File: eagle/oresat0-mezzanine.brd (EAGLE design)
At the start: 80 x 74 mm, 22 parts, among them J1 R107064070, J10 R107064070, J2 R107064070, J3 R107064070, J4 R107064070, J5 R107064070, J6 R107064070, J7 R107064070, J8 R107064070, J9 R107064070, U1 QBA-07+, U2 QBA-07+, U3 QBA-07+, U7 QCN-27D+, U8 QCN-27D+, U9 QCN-27D+

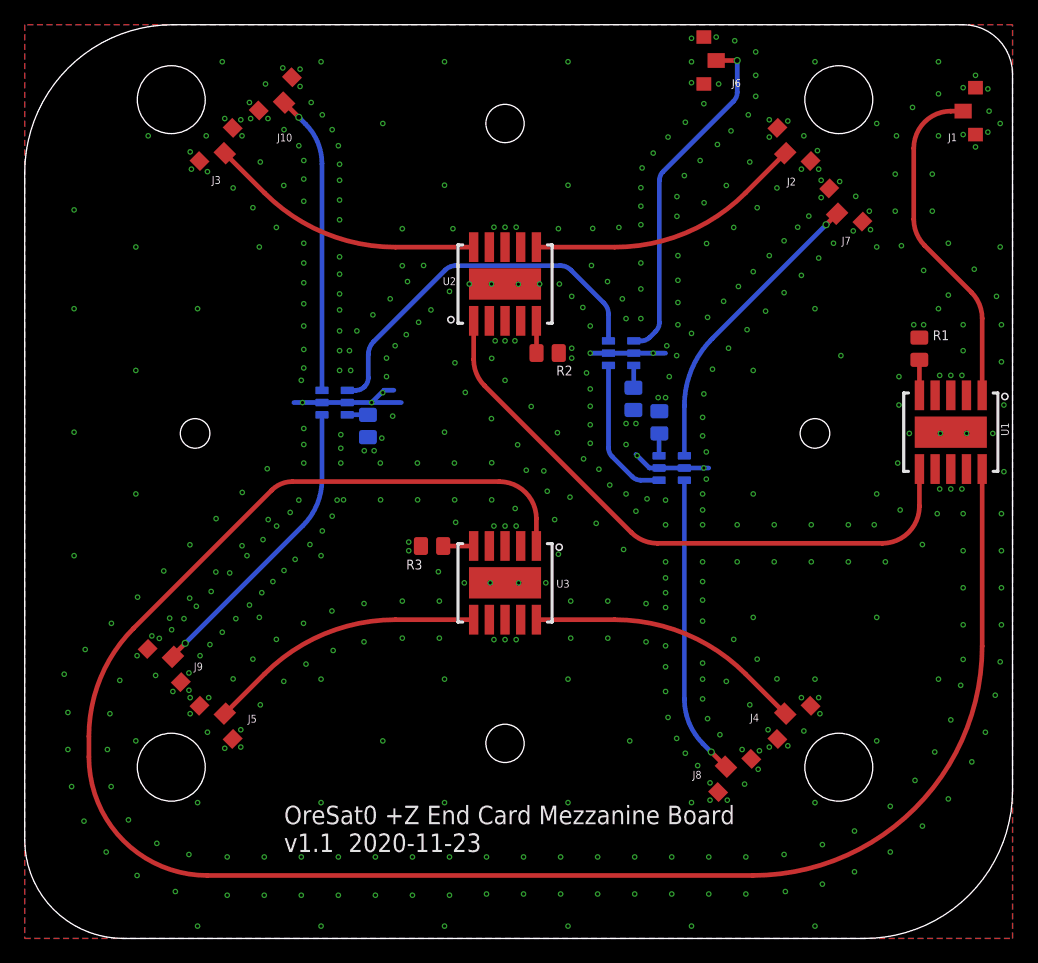
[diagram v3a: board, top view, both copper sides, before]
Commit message: Small tweaks; reduced mezanine board size. Added flight tags. Off to fab!
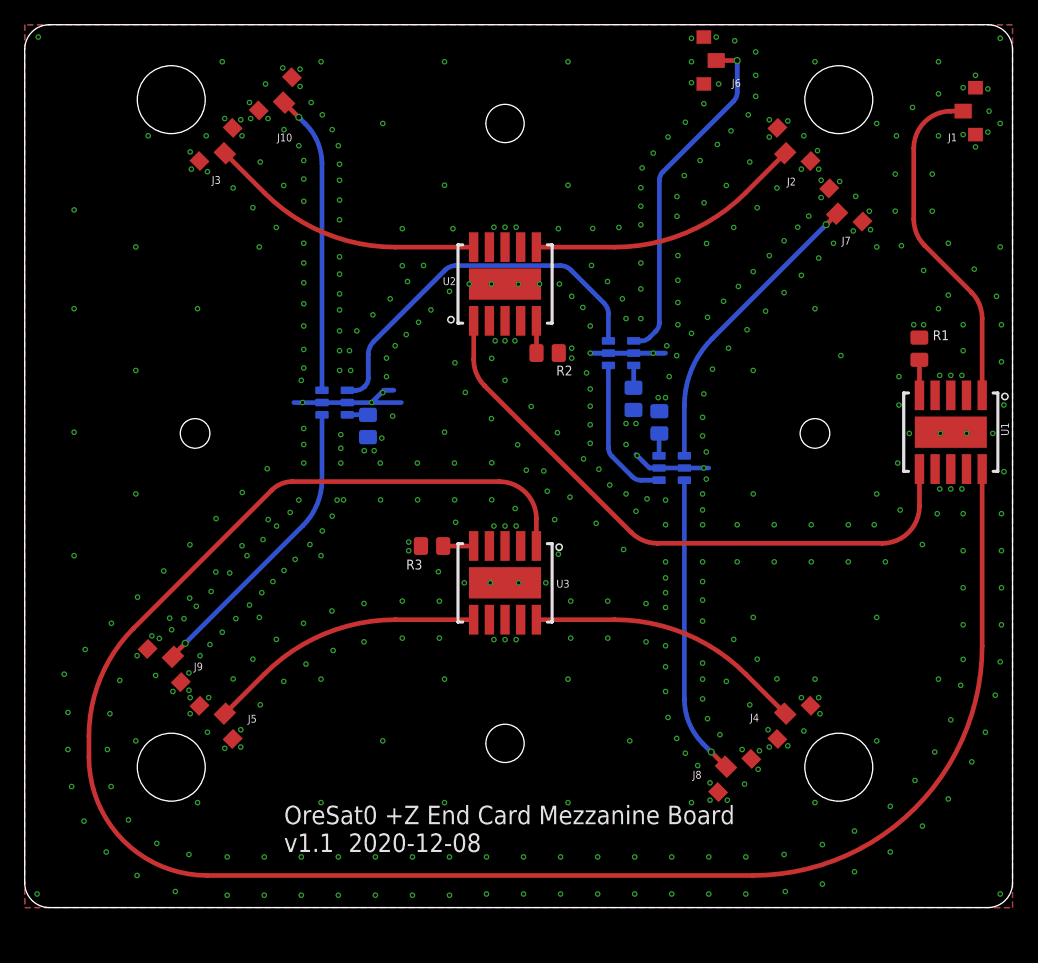
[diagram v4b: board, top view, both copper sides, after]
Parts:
- added U$1: FLIGHMARKERNEW, oresat-flight-marker:FLIGHTMARKER_NEW_BOARDS
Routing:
- net GND: vias 534 -> 532
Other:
- board size 80 x 74 mm -> 80 x 71.5 mm
- board text added: "OreSat0 +Z End Card Mezzanine Board v1.1 2020-12-08"
- board text removed: "OreSat0 +Z End Card Mezzanine Board v1.1 2020-11-23"
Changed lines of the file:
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@@
 <layer number="14" name="Route14" color="22" fill="1" visible="no" active="no"/>
 <layer number="15" name="Route15" color="23" fill="1" visible="no" active="yes"/>
-<layer number="16" name="Bottom" color="1" fill="1" visible="no" active="yes"/>
+<layer number="16" name="Bottom" color="1" fill="1" visible="yes" active="yes"/>
 <layer number="17" name="Pads" color="2" fill="1" visible="yes" active="yes"/>
 <layer number="18" name="Vias" color="2" fill="1" visible="yes" active="yes"/>
@@
 <layer number="20" name="Dimension" color="24" fill="1" visible="yes" active="yes"/>
 <layer number="21" name="tPlace" color="7" fill="1" visible="yes" active="yes"/>
-<layer number="22" name="bPlace" color="7" fill="1" visible="no" active="yes"/>
+<layer number="22" name="bPlace" color="7" fill="1" visible="yes" active="yes"/>
 <layer number="23" name="tOrigins" color="15" fill="1" visible="yes" active="yes"/>
-<layer number="24" name="bOrigins" color="15" fill="1" visible="no" active="yes"/>
+<layer number="24" name="bOrigins" color="15" fill="1" visible="yes" active="yes"/>
 <layer number="25" name="tNames" color="7" fill="1" visible="yes" active="yes"/>
-<layer number="26" name="bNames" color="7" fill="1" visible="no" active="yes"/>
+<layer number="26" name="bNames" color="7" fill="1" visible="yes" active="yes"/>
 <layer number="27" name="tValues" color="7" fill="1" visible="no" active="yes"/>
 <layer number="28" name="bValues" color="7" fill="1" visible="no" active="yes"/>
 <layer number="29" name="tStop" color="7" fill="3" visible="yes" active="yes"/>
-<layer number="30" name="bStop" color="7" fill="6" visible="no" active="yes"/>
+<layer number="30" name="bStop" color="7" fill="6" visible="yes" active="yes"/>
 <layer number="31" name="tCream" color="7" fill="4" visible="no" active="yes"/>
 <layer number="32" name="bCream" color="7" fill="5" visible="no" active="yes"/>
@@
 <board>
 <plain>
-<wire x1="23" y1="82.9" x2="87" y2="82.9" width="0.001" layer="20"/>
-<wire x1="87" y1="82.9" x2="91" y2="78.9" width="0.001" layer="20" curve="-90"/>
-<wire x1="91" y1="78.9" x2="91" y2="20.9" width="0.001" layer="20"/>
-<wire x1="91" y1="20.9" x2="79" y2="8.9" width="0.001" layer="20" curve="-90"/>
-<wire x1="79" y1="8.9" x2="19" y2="8.9" width="0.001" layer="20"/>
-<wire x1="19" y1="8.9" x2="11" y2="16.9" width="0.001" layer="20" curve="-90"/>
-<wire x1="11" y1="16.9" x2="11" y2="70.9" width="0.001" layer="20"/>
-<wire x1="11" y1="70.9" x2="23" y2="82.9" width="0.001" layer="20" curve="-90"/>
+<wire x1="13" y1="82.9" x2="89" y2="82.9" width="0.001" layer="20"/>
+<wire x1="89" y1="82.9" x2="91" y2="80.9" width="0.001" layer="20" curve="-90"/>
+<wire x1="91" y1="80.9" x2="91" y2="13.4" width="0.001" layer="20"/>
+<wire x1="91" y1="13.4" x2="89" y2="11.4" width="0.001" layer="20" curve="-90"/>
+<wire x1="89" y1="11.4" x2="13" y2="11.4" width="0.001" layer="20"/>
+<wire x1="13" y1="11.4" x2="11" y2="13.4" width="0.001" layer="20" curve="-90"/>
+<wire x1="11" y1="13.4" x2="11" y2="80.9" width="0.001" layer="20"/>
+<wire x1="11" y1="80.9" x2="13" y2="82.9" width="0.001" layer="20" curve="-90"/>
 <wire x1="85" y1="75.7" x2="83" y2="72.9" width="2" layer="29" curve="70"/>
 <wire x1="83" y1="72.9" x2="83" y2="67.142640625" width="2" layer="29"/>
@@
 <circle x="75" y="49.8" radius="3" width="0" layer="30"/>
 <text x="32" y="15.9" size="1.5" layer="25" font="vector" ratio="10">OreSat0 +Z End Card Mezzanine Board
-v1.1  2020-11-23</text>
+v1.1  2020-12-08</text>
 <text x="69.4" y="16.2" size="1.5" layer="22" font="vector" ratio="10" rot="MR0">OreSat0 +Z End Card Mezzanine Board
-v1.1  2020-11-23</text>
+v1.1  2020-12-08</text>
 <circle x="22.87" y="76.83" radius="2.75" width="0.001" layer="50"/>
 <circle x="76.93" y="76.83" radius="2.75" width="0.001" layer="50"/>
@@
 <wire x1="27.63138125" y1="74.331359375" x2="25.368640625" y2="72.06861875" width="0.001" layer="50"/>
 <wire x1="8.4" y1="87.68281875" x2="8.4" y2="3.307140625" width="0.001" layer="50"/>
-<wire x1="91.4" y1="12.8" x2="91.4" y2="8.3" width="0.001" layer="50"/>
+<wire x1="91.4" y1="12.8" x2="91.4" y2="10.8" width="0.001" layer="50"/>
 <wire x1="91.4" y1="87.68281875" x2="91.4" y2="3.307140625" width="0.001" layer="50"/>
 <circle x="24.799990625" y="49.799990625" radius="1.2" width="0.001" layer="50"/>
@@
 <circle x="74.999990625" y="49.799990625" radius="1.2" width="0.001" layer="50"/>
 <circle x="49.899990625" y="74.899990625" radius="1.55" width="0.001" layer="50"/>
-<wire x1="91" y1="20.9" x2="91" y2="78.9" width="0.001" layer="50"/>
-<wire x1="91" y1="78.9" x2="87" y2="82.9" width="0.001" layer="50" curve="90"/>
-<wire x1="87" y1="82.9" x2="23" y2="82.9" width="0.001" layer="50"/>
-<wire x1="23" y1="82.9" x2="11" y2="70.9" width="0.001" layer="50" curve="90"/>
-<wire x1="11" y1="70.9" x2="11" y2="16.9" width="0.001" layer="50"/>
-<wire x1="11" y1="16.9" x2="19" y2="8.9" width="0.001" layer="50" curve="90"/>
-<wire x1="19" y1="8.9" x2="79" y2="8.9" width="0.001" layer="50"/>
-<wire x1="79" y1="8.9" x2="91" y2="20.9" width="0.001" layer="50" curve="90"/>
+<wire x1="13" y1="11.4" x2="89" y2="11.4" width="0.001" layer="50"/>
+<wire x1="89" y1="11.4" x2="91" y2="13.4" width="0.001" layer="50" curve="90"/>
+<wire x1="91" y1="13.4" x2="91" y2="80.9" width="0.001" layer="50"/>
+<wire x1="91" y1="80.9" x2="89" y2="82.9" width="0.001" layer="50" curve="90"/>
+<wire x1="89" y1="82.9" x2="13" y2="82.9" width="0.001" layer="50"/>
+<wire x1="13" y1="82.9" x2="11" y2="80.9" width="0.001" layer="50" curve="90"/>
+<wire x1="11" y1="80.9" x2="11" y2="13.4" width="0.001" layer="50"/>
+<wire x1="11" y1="13.4" x2="13" y2="11.4" width="0.001" layer="50" curve="90"/>
 <hole x="76.93" y="76.83" drill="5.5" locked="yes"/>
 <hole x="22.87" y="76.83" drill="5.5" locked="yes"/>
@@
 <attribute name="VALUE" x="37.5" y="49" size="0.6096" layer="28" font="vector" ratio="15" rot="MR0"/>
 </element>
+<element name="U$1" library="oresat-flight-marker" package="FLIGHTMARKER_NEW_BOARDS" value="FLIGHMARKERNEW" x="12.1" y="28.9" smashed="yes" rot="MR90"/>
 </elements>
 <signals>
@@
 <polygon width="0.127" layer="1" isolate="0.2" thermals="no" rank="6">
 <vertex x="11" y="82.9"/>
-<vertex x="11" y="8.9"/>
-<vertex x="91" y="8.9"/>
+<vertex x="11" y="11.4"/>
+<vertex x="91" y="11.4"/>
 <vertex x="91" y="82.9"/>
 </polygon>
@@
 <polygon width="0.127" layer="2" isolate="0.2" thermals="no" rank="6">
 <vertex x="11" y="82.9"/>
-<vertex x="11" y="8.9"/>
-<vertex x="91" y="8.9"/>
+<vertex x="11" y="11.4"/>
+<vertex x="91" y="11.4"/>
 <vertex x="91" y="82.9"/>
 </polygon>
 <polygon width="0.127" layer="15" isolate="0.2" thermals="no" rank="6">
 <vertex x="11" y="82.9"/>
-<vertex x="11" y="8.9"/>
-<vertex x="91" y="8.9"/>
+<vertex x="11" y="11.4"/>
+<vertex x="91" y="11.4"/>
 <vertex x="91" y="82.9"/>
 </polygon>
 <polygon width="0.127" layer="16" isolate="0.2" thermals="no" rank="6">
 <vertex x="11" y="82.9"/>
-<vertex x="11" y="8.9"/>
-<vertex x="91" y="8.9"/>
+<vertex x="11" y="11.4"/>
+<vertex x="91" y="11.4"/>
 <vertex x="91" y="82.9"/>
 </polygon>
@@
 <via x="80" y="24.9" extent="1-16" drill="0.254"/>
 <via x="85" y="29.9" extent="1-16" drill="0.254"/>
-<via x="75" y="9.9" extent="1-16" drill="0.254"/>
-<via x="65" y="9.9" extent="1-16" drill="0.254"/>
-<via x="55" y="9.9" extent="1-16" drill="0.254"/>
-<via x="45" y="9.9" extent="1-16" drill="0.254"/>
-<via x="35" y="9.9" extent="1-16" drill="0.254"/>
-<via x="25" y="9.9" extent="1-16" drill="0.254"/>
 <via x="80" y="34.9" extent="1-16" drill="0.254"/>
 <via x="70" y="34.9" extent="1-16" drill="0.254"/>
@@
 <via x="40" y="53.1" extent="1-16" drill="0.254"/>
 <via x="40.8" y="51.2" extent="1-16" drill="0.254"/>
+<via x="12" y="12.5" extent="1-16" drill="0.254"/>
+<via x="90" y="12.5" extent="1-16" drill="0.254"/>
+<via x="90" y="81.8" extent="1-16" drill="0.254"/>
+<via x="12.1" y="81.9" extent="1-16" drill="0.254"/>
 </signal>
 <signal name="UHF" class="1">

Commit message: Version 1.2 of the OreSat0 end card and mezzanine.
Largest change is the position of the antennas on the end card; changes to the deployer changed the antenna placement which triggered everything else.

Other changes include fiducials, attributes cleanup, move to 0603 resistors, and misc polish.
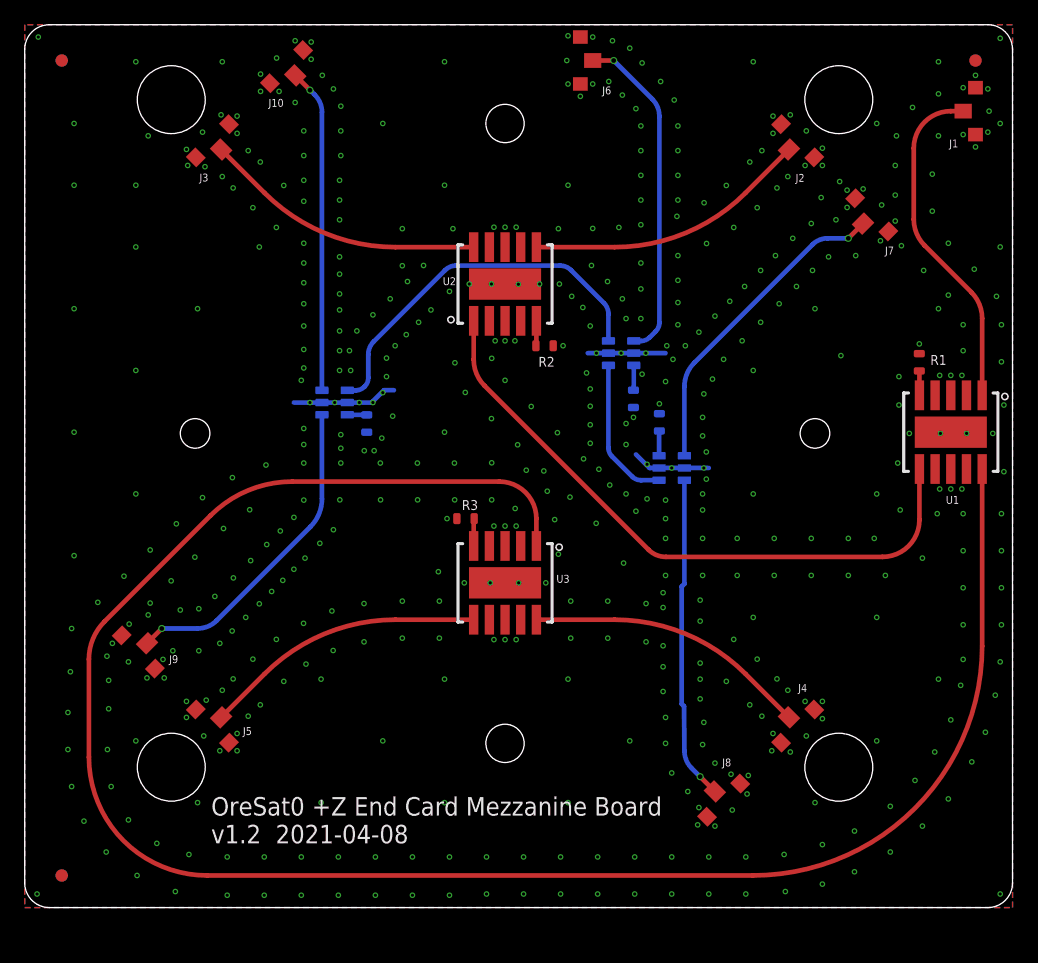
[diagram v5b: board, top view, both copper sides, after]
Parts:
- added FIDUCIAL1, FIDUCIAL2, FIDUCIAL3, FIDUCIAL4, FIDUCIAL6, FIDUCIAL7: FIDUCIAL-1.0X2.0, monitor-v2-debug:FIDUCIAL-1.0X2.0
- R1, R2, R3, R4, R5, R6: device oresat-rcl:.0805-B-NOSILK -> oresat-rcl:.0603-C-NOSILK
- U7, U8, U9: value QCN-27D+ -> QCN-27+
- moved U$1 50.5 mm to (60.2, 13.4), turned to 0 degrees
- moved J6 10.0 mm to (56.0, 80.0)
- moved R3 3.50 mm to (46.7, 42.9)
- moved J10 2.38 mm to (32.2, 79.5)
- moved J9 2.37 mm to (20.2, 32.1)
- moved J7 2.25 mm to (79.6, 67.5)
- moved J8 2.19 mm to (67.6, 20.1)
- moved R1 1.10 mm to (83.5, 55.6)
- moved R2 0.64 mm to (53.1, 56.9)
- moved J3 0.42 mm to (26.2, 73.5)
- moved J5 0.42 mm to (26.2, 26.1)
- moved J2 0.42 mm to (73.6, 73.5)
- moved J4 0.42 mm to (73.6, 26.1)
- moved R6 0.22 mm to (38.7, 50.6)
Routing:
- net GND: track 23.4 -> 21.3 mm, vias 532 -> 538
- net SBAND_270: track 24.3 -> 26.3 mm
- net SBAND_90: track 24.3 -> 26.3 mm
- net SBAND_180: track 24.3 -> 26.3 mm
- net UHF-SHORT+1/4WAVE: track 150.3 -> 152.1 mm
- net SBAND_0: track 24.2 -> 25.9 mm
- net UHF-SHORT: track 50.0 -> 51.6 mm
- net SBAND: track 28.2 -> 27.1 mm
- net N$3: track 2.88 -> 1.98 mm
- net N$4: track 2.61 -> 2.03 mm
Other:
- board text added: "OreSat0 +Z End Card Mezzanine Board v1.2 2021-04-08"
- board text removed: "OreSat0 +Z End Card Mezzanine Board v1.1 2020-12-08"

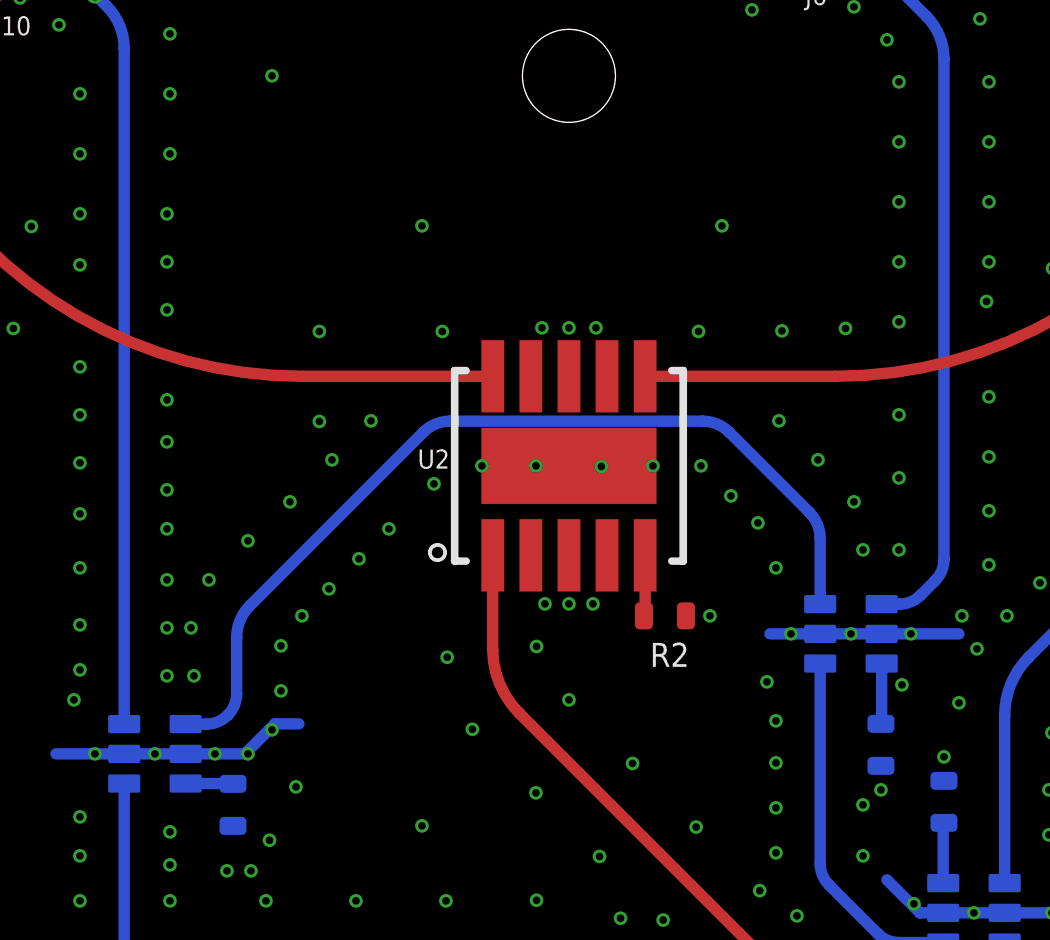
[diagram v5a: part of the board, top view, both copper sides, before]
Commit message: replaced S-band net labels with L1-band labels, swapped the S-band hybrids with L-band hybrids, recalculated 1/4 wavelength trace length, routed a new short+1/4 wavelength trace
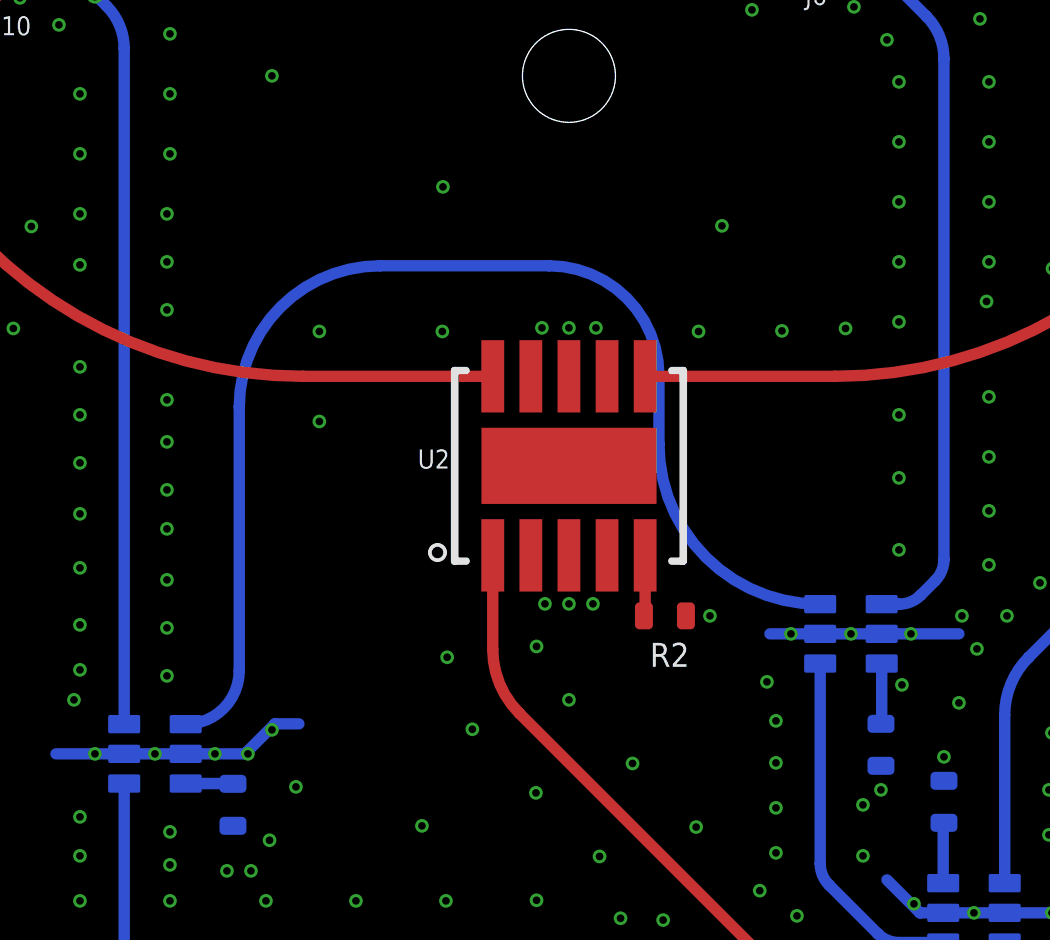
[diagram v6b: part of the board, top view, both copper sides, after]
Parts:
- U7, U8, U9: value QCN-27+ -> QCN-19+
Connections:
- net SBAND renamed L1BAND
- net SBAND-SHORT renamed L1BAND-SHORT
- net SBAND-SHORT+1/4WAVE renamed L1BAND-SHORT+1/4WAVE
- net SBAND_0 renamed L1BAND_0
- net SBAND_180 renamed L1BAND_180
- net SBAND_270 renamed L1BAND_270
- net SBAND_90 renamed L1BAND_90
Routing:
- net L1BAND-SHORT+1/4WAVE: track 30.7 -> 38.7 mm
- net GND: vias 538 -> 512
